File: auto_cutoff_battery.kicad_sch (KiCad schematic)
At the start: 33 parts, among them J1 RJ45, J2 RJ45, Q1 IRF540N, Q2 IRF9540N, U1 L7805, U2 PC817, U3 PC817, U4 PC817

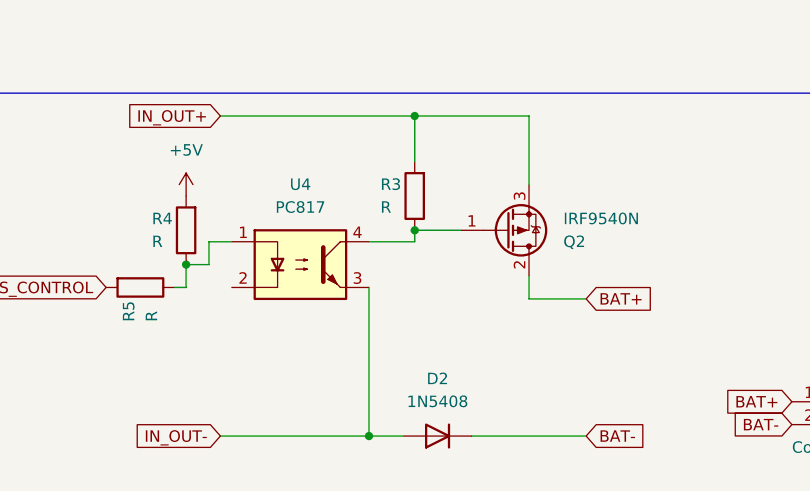
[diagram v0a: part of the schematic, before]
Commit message: minor change in power electronics schematic
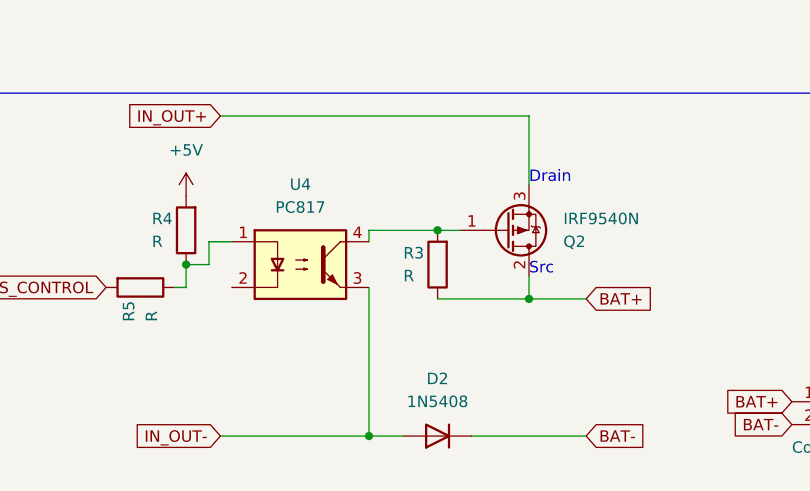
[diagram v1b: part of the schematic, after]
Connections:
- net BAT+: now also R3.1
- net IN_OUT+: no longer R3.2
- net at Q2.1 (G), U4.4: now also R3.2; no longer R3.1
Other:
- note added: "Drain"
- note added: "Src"
- moved on the sheet: R3
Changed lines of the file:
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@@
   (junction (at 154.94 88.9) (diameter 0) (color 0 0 0 0)
   )
-  (junction (at 205.74 22.86) (diameter 0) (color 0 0 0 0)
-  )
   (junction (at 205.74 83.82) (diameter 0) (color 0 0 0 0)
   )
-  (junction (at 205.74 35.56) (diameter 0) (color 0 0 0 0)
+  (junction (at 218.44 43.18) (diameter 0) (color 0 0 0 0)
+  )
+  (junction (at 208.28 35.56) (diameter 0) (color 0 0 0 0)
   )
   (junction (at 205.74 100.33) (diameter 0) (color 0 0 0 0)
@@
     (stroke (width 0) (type default))
   )
-  (wire (pts (xy 205.74 35.56) (xy 205.74 36.83))
-    (stroke (width 0) (type default))
-  )
   (wire (pts (xy 200.66 58.42) (xy 204.47 58.42))
     (stroke (width 0) (type default))
@@
     (stroke (width 0) (type default))
   )
+  (wire (pts (xy 208.28 35.56) (xy 200.66 35.56))
+    (stroke (width 0) (type default))
+  )
   (wire (pts (xy 205.74 102.87) (xy 201.93 102.87))
     (stroke (width 0) (type default))
@@
     (stroke (width 0) (type default))
   )
-  (wire (pts (xy 205.74 22.86) (xy 218.44 22.86))
-    (stroke (width 0) (type default))
-  )
   (wire (pts (xy 182.88 36.83) (xy 182.88 39.37))
     (stroke (width 0) (type default))
@@
     (stroke (width 0) (type default))
   )
-  (wire (pts (xy 200.66 36.83) (xy 205.74 36.83))
-    (stroke (width 0) (type default))
-  )
   (wire (pts (xy 184.15 83.82) (xy 205.74 83.82))
     (stroke (width 0) (type default))
   )
+  (wire (pts (xy 200.66 35.56) (xy 200.66 36.83))
+    (stroke (width 0) (type default))
+  )
   (wire (pts (xy 224.79 93.98) (xy 218.44 93.98))
     (stroke (width 0) (type default))
@@
     (stroke (width 0) (type default))
   )
-  (wire (pts (xy 184.15 22.86) (xy 205.74 22.86))
+  (wire (pts (xy 184.15 22.86) (xy 218.44 22.86))
     (stroke (width 0) (type default))
   )
@@
     (stroke (width 0) (type default))
   )
-  (wire (pts (xy 205.74 22.86) (xy 205.74 27.94))
-    (stroke (width 0) (type default))
-  )
   (wire (pts (xy 218.44 118.11) (xy 218.44 105.41))
     (stroke (width 0) (type default))
@@
     (stroke (width 0) (type default))
   )
-  (wire (pts (xy 205.74 35.56) (xy 210.82 35.56))
+  (wire (pts (xy 210.82 35.56) (xy 208.28 35.56))
     (stroke (width 0) (type default))
   )
@@
     (stroke (width 0) (type default))
   )
+  (wire (pts (xy 208.28 43.18) (xy 218.44 43.18))
+    (stroke (width 0) (type default))
+  )
   (wire (pts (xy 185.42 36.83) (xy 182.88 36.83))
     (stroke (width 0) (type default))
@@
     (stroke (width 0) (type default))
     (fill (type none))
+  )
+  (text "Drain\n" (at 218.44 30.48 0)
+    (effects (font (size 1.27 1.27)) (justify left bottom))
   )
   (text "Control Circuit\n" (at 26.67 35.56 0)
     (effects (font (size 5 5)) (justify left bottom))
+  )
+  (text "Src" (at 218.44 40.64 0)
+    (effects (font (size 1.27 1.27)) (justify left bottom))
   )
   (text "Power Circuit" (at 107.95 20.32 0)
@@
     )
   )
-  (symbol (lib_id "Device:R") (at 205.74 31.75 180) (unit 1)
+  (symbol (lib_id "Device:R") (at 208.28 39.37 180) (unit 1)
     (in_bom yes) (on_board yes) (dnp no)
-    (property "Reference" "R3" (at 201.93 30.48 0)
+    (property "Reference" "R3" (at 204.47 38.1 0)
       (effects (font (size 1.27 1.27)) (justify right))
     )
-    (property "Value" "R" (at 201.93 33.02 0)
+    (property "Value" "R" (at 204.47 40.64 0)
       (effects (font (size 1.27 1.27)) (justify right))
     )
-    (property "Footprint" "Resistor_THT:R_Axial_DIN0207_L6.3mm_D2.5mm_P7.62mm_Horizontal" (at 207.518 31.75 90)
-      (effects (font (size 1.27 1.27)) hide)
-    )
-    (property "Datasheet" "~" (at 205.74 31.75 0)
-      (effects (font (size 1.27 1.27)) hide)
-    )
+    (property "Footprint" "Resistor_THT:R_Axial_DIN0207_L6.3mm_D2.5mm_P7.62mm_Horizontal" (at 210.058 39.37 90)
+      (effects (font (size 1.27 1.27)) hide)
+    )
+    (property "Datasheet" "~" (at 208.28 39.37 0)
+      (effects (font (size 1.27 1.27)) hide)
+    )

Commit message: minor changes
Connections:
- net NMOS_CONTROL renamed not NMOS_CONTROL
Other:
- note added: "Charging"
- note added: "Discharging"
- moved on the sheet: IN_OUT
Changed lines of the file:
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@@
     (stroke (width 0) (type default))
+  )
+  (rectangle (start 160.02 76.2) (end 234.95 120.65)
+    (stroke (width 0) (type default))
+    (fill (type none))
+  )
+  (rectangle (start 152.4 21.59) (end 237.49 62.23)
+    (stroke (width 0) (type default))
+    (fill (type none))
   )
   (rectangle (start 105.41 20.32) (end 265.43 123.19)
@@
     (fill (type none))
   )
+  (text "Discharging" (at 156.21 34.29 0)
+    (effects (font (size 2 2)) (justify left bottom))
+  )
   (text "Drain\n" (at 218.44 30.48 0)
     (effects (font (size 1.27 1.27)) (justify left bottom))
@@
     (effects (font (size 5 5)) (justify left bottom))
   )
+  (text "Src" (at 214.63 106.68 0)
+    (effects (font (size 1.27 1.27)) (justify left bottom))
+  )
+  (text "Drain\n" (at 219.71 93.98 0)
+    (effects (font (size 1.27 1.27)) (justify left bottom))
+  )
+  (text "Charging" (at 165.1 92.71 0)
+    (effects (font (size 2 2)) (justify left bottom))
+  )
   (text "Src" (at 218.44 40.64 0)
     (effects (font (size 1.27 1.27)) (justify left bottom))
@@
     )
   )
+  (global_label "not NMOS_CONTROL" (shape input) (at 46.99 80.01 180) (fields_autoplaced)
+    (effects (font (size 1.27 1.27)) (justify right))
+    (property "Intersheetrefs" "${INTERSHEET_REFS}" (at 25.1968 80.01 0)
+      (effects (font (size 1.27 1.27)) (justify right) hide)
+    )
+  )
   (global_label "IN_OUT+" (shape input) (at 184.15 83.82 180) (fields_autoplaced)
     (effects (font (size 1.27 1.27)) (justify right))
@@
     )
   )
-  (global_label "NMOS_CONTROL" (shape input) (at 45.72 80.01 180) (fields_autoplaced)
-    (effects (font (size 1.27 1.27)) (justify right))
-    (property "Intersheetrefs" "${INTERSHEET_REFS}" (at 27.9181 80.01 0)
-      (effects (font (size 1.27 1.27)) (justify right) hide)
-    )
-  )
   (global_label "IN_OUT REF" (shape input) (at 123.19 88.9 180) (fields_autoplaced)
     (effects (font (size 1.27 1.27)) (justify right))
@@
     )
   )
-  (global_label "IN_OUT-" (shape input) (at 143.51 58.42 0) (fields_autoplaced)
-    (effects (font (size 1.27 1.27)) (justify left))
-    (property "Intersheetrefs" "${INTERSHEET_REFS}" (at 154.5991 58.42 0)
+  (global_label "IN_OUT-" (shape input) (at 135.89 58.42 0) (fields_autoplaced)
+    (effects (font (size 1.27 1.27)) (justify left))
+    (property "Intersheetrefs" "${INTERSHEET_REFS}" (at 146.9791 58.42 0)
       (effects (font (size 1.27 1.27)) (justify left) hide)
     )
@@
     )
   )
-  (global_label "IN_OUT+" (shape input) (at 143.51 55.88 0) (fields_autoplaced)
-    (effects (font (size 1.27 1.27)) (justify left))
-    (property "Intersheetrefs" "${INTERSHEET_REFS}" (at 154.5991 55.88 0)
+  (global_label "IN_OUT+" (shape input) (at 135.89 55.88 0) (fields_autoplaced)
+    (effects (font (size 1.27 1.27)) (justify left))
+    (property "Intersheetrefs" "${INTERSHEET_REFS}" (at 146.9791 55.88 0)
       (effects (font (size 1.27 1.27)) (justify left) hide)
     )
@@
     )
   )
-  (global_label "NMOS_CONTROL" (shape input) (at 179.07 102.87 180) (fields_autoplaced)
-    (effects (font (size 1.27 1.27)) (justify right))
-    (property "Intersheetrefs" "${INTERSHEET_REFS}" (at 161.2681 102.87 0)
+  (global_label "not NMOS_CONTROL" (shape input) (at 179.07 102.87 180) (fields_autoplaced)
+    (effects (font (size 1.27 1.27)) (justify right))
+    (property "Intersheetrefs" "${INTERSHEET_REFS}" (at 157.2768 102.87 0)
       (effects (font (size 1.27 1.27)) (justify right) hide)
     )
@@
     )
   )
-  (symbol (lib_id "Connector_Generic:Conn_02x03_Counter_Clockwise") (at 133.35 58.42 0) (unit 1)
-    (in_bom yes) (on_board yes) (dnp no) (fields_autoplaced)
-    (property "Reference" "IN_OUT" (at 134.62 49.53 0)
-      (effects (font (size 1.27 1.27)))
-    )
-    (property "Value" "Conn_02x03_Counter_Clockwise" (at 134.62 52.07 0)
-      (effects (font (size 1.27 1.27)))
-    )
-    (property "Footprint" "Connector_PinSocket_2.54mm:PinSocket_2x03_P2.54mm_Vertical" (at 133.35 58.42 0)
-      (effects (font (size 1.27 1.27)) hide)
-    )
-    (property "Datasheet" "~" (at 133.35 58.42 0)
-      (effects (font (size 1.27 1.27)) hide)
-    )
+  (symbol (lib_id "Connector_Generic:Conn_02x03_Counter_Clockwise") (at 125.73 58.42 0) (unit 1)
+    (in_bom yes) (on_board yes) (dnp no) (fields_autoplaced)
+    (property "Reference" "IN_OUT" (at 127 49.53 0)
+      (effects (font (size 1.27 1.27)))
+    )
+    (property "Value" "Conn_02x03_Counter_Clockwise" (at 127 52.07 0)
+      (effects (font (size 1.27 1.27)))
+    )
+    (property "Footprint" "Connector_PinSocket_2.54mm:PinSocket_2x03_P2.54mm_Vertical" (at 125.73 58.42 0)
+      (effects (font (size 1.27 1.27)) hide)
+    )
+    (property "Datasheet" "~" (at 125.73 58.42 0)
+      (effects (font (size 1.27 1.27)) hide)
+    )

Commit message: started PCB design
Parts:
- removed C1: C, Capacitor_THT:C_Disc_D5.0mm_W2.5mm_P2.50mm, symbol Device:C
- removed Debugging: Conn_01x03_Socket, Connector_PinSocket_2.54mm:PinSocket_1x03_P2.54mm_Vertical, symbol Connector:Conn_01x03_Socket
- removed STC15W408AS: Conn_02x08_Counter_Clockwise, Package_DIP:DIP-16_W7.62mm_LongPads, symbol Connector_Generic:Conn_02x08_Counter_Clockwise
- removed U1: L7805, symbol Regulator_Linear:L7805
- added Q10, Q3, Q4, Q5, Q6, Q7, Q8, Q9: S8050, Package_TO_SOT_THT:TO-92_Inline_Wide, symbol Transistor_BJT:S8050
- added R13, R14, R15, R16, R17, R18, R19, R20, R21, R22, R23: R, Resistor_THT:R_Axial_DIN0207_L6.3mm_D2.5mm_P7.62mm_Horizontal, symbol Device:R
- added U1, U5: TL431LP, Package_TO_SOT_THT:TO-92_Inline_Wide, symbol Reference_Voltage:TL431LP
- renumbered BAT to BAT1, IN_OUT to IN_OUT1
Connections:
- net +5V: no longer R12.1
- net BAT+: now also R12.1, R2.1, R14.2, R15.1, R17.1, R19.2, R20.2, R21.2, R22.2, R23.2
- net BAT-: now also R9.2, U2.3, U3.2, U4.2, Q10.1 (E), Q3.1 (E), Q4.1 (E), Q5.1 (E), Q6.1 (E), Q8.1 (E), Q9.1 (E), R16.2, U1.2 (A), U5.2 (A); no longer R2.2
- net IN_OUT-: no longer R9.2
- net PMOS_CONTROL: now also Q10.3 (C), R23.1
- net not NMOS_CONTROL: now also Q9.3 (C), R21.1
- net at R8.2, U2.1: no longer R9.1
- net BAT+ REF: no longer names the net of R1.2
- net BAT+ REF: now also R13.1, U1.3 (K); no longer R2.1
- net IN_OUT REF: no longer names the net of R12.2, U2.4
- net IN_OUT REF: now also Q6.2 (B), Q8.2 (B)
- new net: R17.2, R18.1, U5.3 (K)
- new net: Q4.2 (B), R18.2
- new net: Q7.1 (E), Q8.3 (C)
- new net: Q3.3 (C), Q7.2 (B), R14.1
- new net: Q10.2 (B), Q7.3 (C), R22.1
- new net: Q4.3 (C), Q5.2 (B), R19.1
- new net: Q5.3 (C), Q6.3 (C), Q9.2 (B), R20.1
- new net: R2.2, R9.1, U1.1 (REF)
- new net: Q3.2 (B), R13.2
- new net: R15.2, R16.1, U5.1 (REF)
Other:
- note added: "!(V_bat < V_max_bat)"
- note added: "!(V_bat < V_min_bat)"
- note added: "!(V_in_out)"
- moved on the sheet: BAT1, D1, D2, D3, D4, H1, H2, H3, H4, IN_OUT1, J1, J2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

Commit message: finished PCB solution
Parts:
- removed BAT1: Conn_01x02_Socket, Connector_PinSocket_2.54mm:PinSocket_1x02_P2.54mm_Vertical, symbol Connector:Conn_01x02_Socket
- added Bridge1, Bridge2, Bridge3: R, Resistor_THT:R_Axial_DIN0207_L6.3mm_D2.5mm_P5.08mm_Vertical, symbol Device:R
- added Bridge4: R, Resistor_THT:R_Axial_DIN0207_L6.3mm_D2.5mm_P15.24mm_Horizontal, symbol Device:R
- added J3, J4: Conn_01x01_Socket, Connector_PinSocket_2.54mm:PinSocket_1x01_P2.54mm_Vertical, symbol Connector:Conn_01x01_Socket
- D4: value GREEN_LED -> YELLOW_LED
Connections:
- net +5V is gone; now on net BAT+: R4.2
- net BAT+: now also Bridge4.1, Bridge4.2, J3.1 (Pin_1)
- net BAT-: now also Bridge2.1, Bridge2.2, J4.1 (Pin_1)
- net IN_OUT+: now also IN_OUT1.6 (Pin_6)
- net IN_OUT-: now also IN_OUT1.5 (Pin_5), Bridge3.1, Bridge3.2
- net at Q4.3 (C), R19.1: now also Bridge1.1; no longer Q5.2 (B)
- net at Q8.2 (B), R12.2, U2.4: now also Q5.2 (B); no longer Q6.2 (B)
- net at R10.1: now also D4.1 (K); no longer D4.2 (A)
- net at R11.1: now also D3.1 (K); no longer D3.2 (A)
- new net: Bridge1.2, Q6.2 (B)
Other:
- moved on the sheet: D3, D4, Q10, Q3, Q4, Q5, Q6, Q7, Q8, Q9, R1, R10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

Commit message: finished PCB and added gcode files
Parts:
- removed IN_OUT1: Conn_02x03_Counter_Clockwise, Connector_PinSocket_2.54mm:PinSocket_2x03_P2.54mm_Vertical, symbol Connector_Generic:Conn_02x03_Counter_Clockwise
- added J5, J6: Conn_01x03_Socket, Connector_Wire:SolderWire-0.1sqmm_1x03_P3.6mm_D0.4mm_OD1mm, symbol Connector:Conn_01x03_Socket
- Bridge4: footprint Resistor_THT:R_Axial_DIN0207_L6.3mm_D2.5mm_P15.24mm_Horizontal -> Resistor_THT:R_Axial_DIN0207_L6.3mm_D2.5mm_P7.62mm_Horizontal
- H1, H2, H3, H4: footprint MountingHole:MountingHole_3.2mm_M3_ISO7380_Pad -> MountingHole:MountingHole_5.3mm_M5_DIN965_Pad
- J1, J2: footprint (none) -> Connector_RJ:RJ45_Molex_0855135013_Vertical
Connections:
- net IN_OUT+: now also J6.3 (Pin_3)
- net IN_OUT-: now also J5.1 (Pin_1)

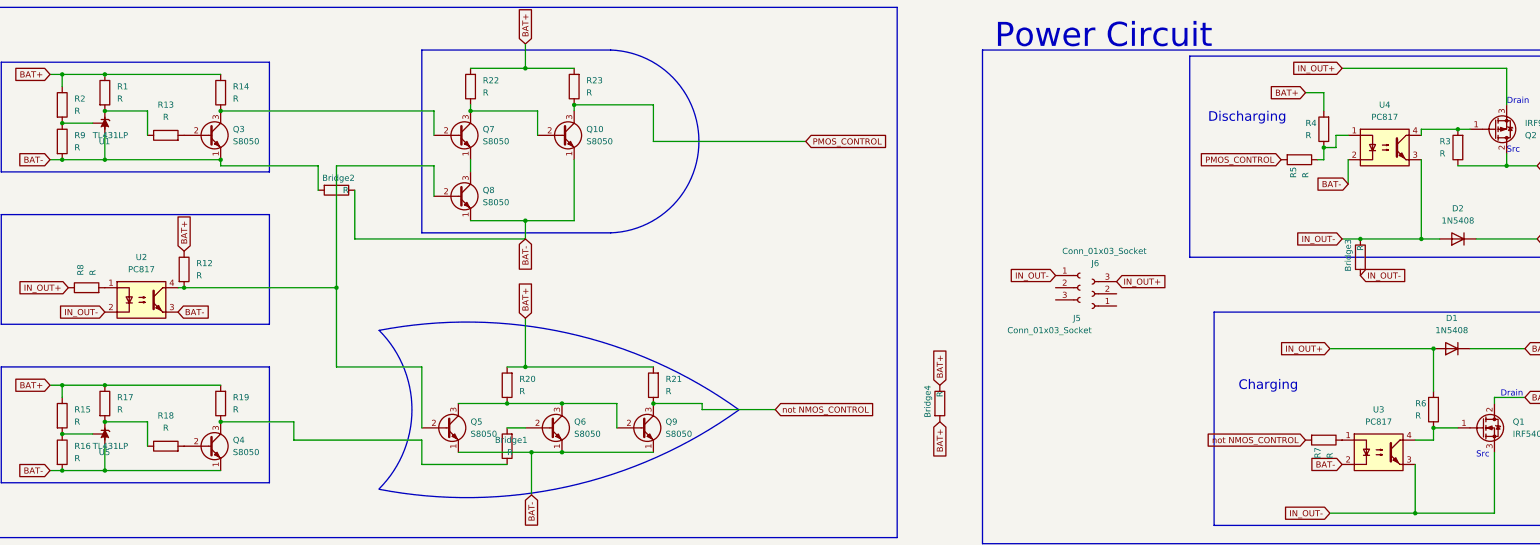
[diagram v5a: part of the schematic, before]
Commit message: added resistor values
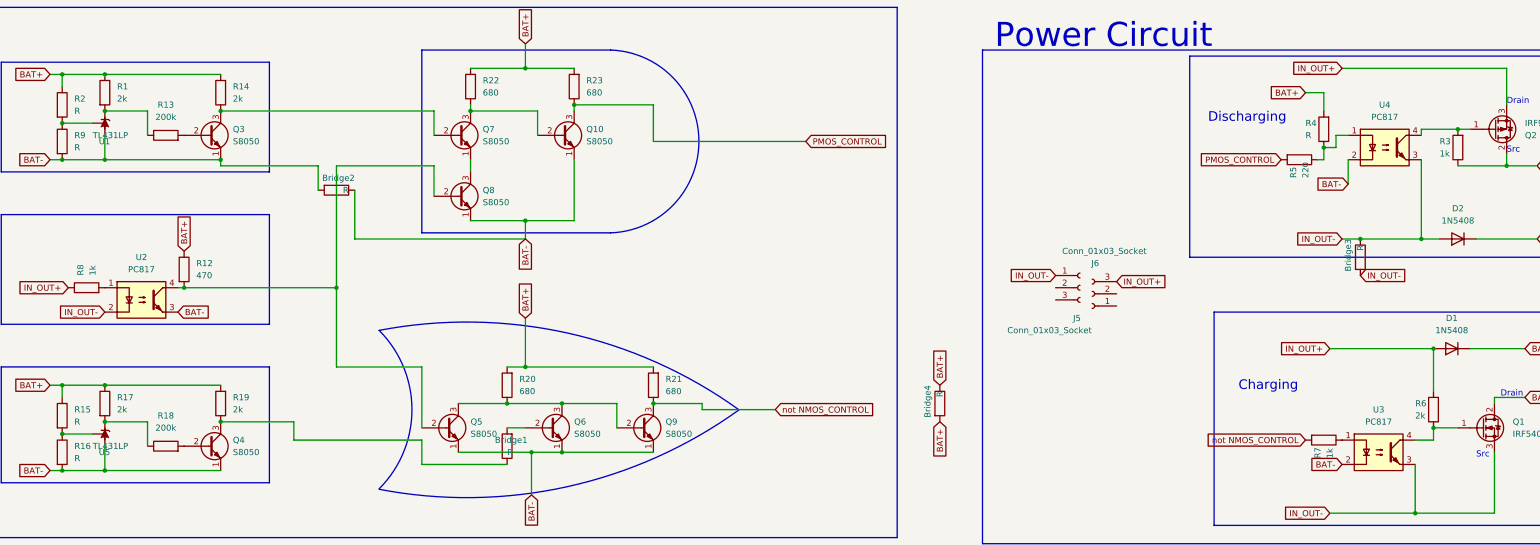
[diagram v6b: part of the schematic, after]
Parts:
- R1, R14, R17, R19, R6: value R -> 2k
- R12: value R -> 470
- R13, R18: value R -> 200k
- R20, R21, R22, R23: value R -> 680
- R3, R7, R8: value R -> 1k
- R5: value R -> 220
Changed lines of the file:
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@@
       (effects (font (size 1.27 1.27)))
     )
-    (property "Value" "R" (at -133.35 -30.48 90)
+    (property "Value" "200k" (at -133.35 -30.48 90)
       (effects (font (size 1.27 1.27)))
     )
@@
       (effects (font (size 1.27 1.27)) (justify left))
     )
-    (property "Value" "R" (at -148.59 -62.23 0)
+    (property "Value" "1k" (at -148.59 -62.23 0)
       (effects (font (size 1.27 1.27)) (justify left))
     )
@@
       (effects (font (size 1.27 1.27)))
     )
-    (property "Value" "R" (at -133.35 -95.25 90)
+    (property "Value" "200k" (at -133.35 -95.25 90)
       (effects (font (size 1.27 1.27)))
     )
@@
       (effects (font (size 1.27 1.27)) (justify right))
     )
-    (property "Value" "R" (at 109.22 -24.13 0)
+    (property "Value" "1k" (at 109.22 -24.13 0)
       (effects (font (size 1.27 1.27)) (justify right))
     )
@@
       (effects (font (size 1.27 1.27)) (justify left))
     )
-    (property "Value" "R" (at -143.51 -99.06 0)
+    (property "Value" "2k" (at -143.51 -99.06 0)
       (effects (font (size 1.27 1.27)) (justify left))
     )
@@
       (effects (font (size 1.27 1.27)) (justify right))
     )
-    (property "Value" "R" (at -67.31 -100.33 0)
+    (property "Value" "680" (at -67.31 -100.33 0)
       (effects (font (size 1.27 1.27)) (justify right))
     )
@@
       (effects (font (size 1.27 1.27)) (justify right))
     )
-    (property "Value" "R" (at -45.72 -100.33 0)
+    (property "Value" "680" (at -45.72 -100.33 0)
       (effects (font (size 1.27 1.27)) (justify right))
     )
@@
       (effects (font (size 1.27 1.27)) (justify right))
     )
-    (property "Value" "R" (at -29.21 -38.1 0)
+    (property "Value" "680" (at -29.21 -38.1 0)
       (effects (font (size 1.27 1.27)) (justify right))
     )
@@
       (effects (font (size 1.27 1.27)) (justify right))
     )
-    (property "Value" "R" (at 132.08 -87.63 0)
+    (property "Value" "1k" (at 132.08 -87.63 0)
       (effects (font (size 1.27 1.27)) (justify right))
     )
@@
       (effects (font (size 1.27 1.27)) (justify right))
     )
-    (property "Value" "R" (at 127 -33.02 0)
+    (property "Value" "2k" (at 127 -33.02 0)
       (effects (font (size 1.27 1.27)) (justify right))
     )
@@
       (effects (font (size 1.27 1.27)) (justify right))
     )
-    (property "Value" "R" (at -119.38 -34.29 0)
+    (property "Value" "2k" (at -119.38 -34.29 0)
       (effects (font (size 1.27 1.27)) (justify right))
     )
@@
       (effects (font (size 1.27 1.27)) (justify right))
     )
-    (property "Value" "R" (at -59.69 -38.1 0)
+    (property "Value" "680" (at -59.69 -38.1 0)
       (effects (font (size 1.27 1.27)) (justify right))
     )
@@
   )
   (symbol (lib_id "Device:R") (at -129.54 -63.5 0) (unit 1)
-    (in_bom yes) (on_board yes) (dnp no) (fields_autoplaced)
+    (in_bom yes) (on_board yes) (dnp no)
     (property "Reference" "R12" (at -127 -64.77 0)
       (effects (font (size 1.27 1.27)) (justify left))
     )
-    (property "Value" "R" (at -127 -62.23 0)
+    (property "Value" "470" (at -127 -62.23 0)
       (effects (font (size 1.27 1.27)) (justify left))
     )
@@
       (effects (font (size 1.27 1.27)) (justify right))
     )
-    (property "Value" "R" (at -119.38 -99.06 0)
+    (property "Value" "2k" (at -119.38 -99.06 0)
       (effects (font (size 1.27 1.27)) (justify right))
     )
@@
       (effects (font (size 1.27 1.27)) (justify right))
     )
-    (property "Value" "R" (at 104.14 -82.55 0)
+    (property "Value" "220" (at 104.14 -82.55 0)
       (effects (font (size 1.27 1.27)) (justify right))
     )
@@
       (effects (font (size 1.27 1.27)) (justify left))
     )
-    (property "Value" "R" (at -143.51 -34.29 0)
-      (effects (font (size 1.27 1.27)) (justify left))
-    )
+    (property "Value" "2k" (at -143.51 -34.29 0)
+      (effects (font (size 1.27 1.27)) (justify left))
+    )
